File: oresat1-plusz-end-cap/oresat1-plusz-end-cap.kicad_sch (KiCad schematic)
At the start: 44 parts, among them J1 M55-7011242R, J2 U.FL-R-SMA, U1 RM3100, U2 RM3100

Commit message: routine push
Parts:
- added R16, R17, R18, R19: 121, oresat-passives:0603-C-NOSILK, symbol oresat-passives:R-US

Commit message: routine push
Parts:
- R17, R18: now not fitted
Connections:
- net +3.3v: now also R18.1, R19.1; no longer U1.28 (MISO/SA1)
- net GND: now also R16.2, R17.2; no longer U1.3 (SSN/SA0)
- net at R18.2: now also R16.1, U1.28 (MISO/SA1)
- net at R17.1: now also R19.2, U1.3 (SSN/SA0)
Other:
- moved on the sheet: R16, R19

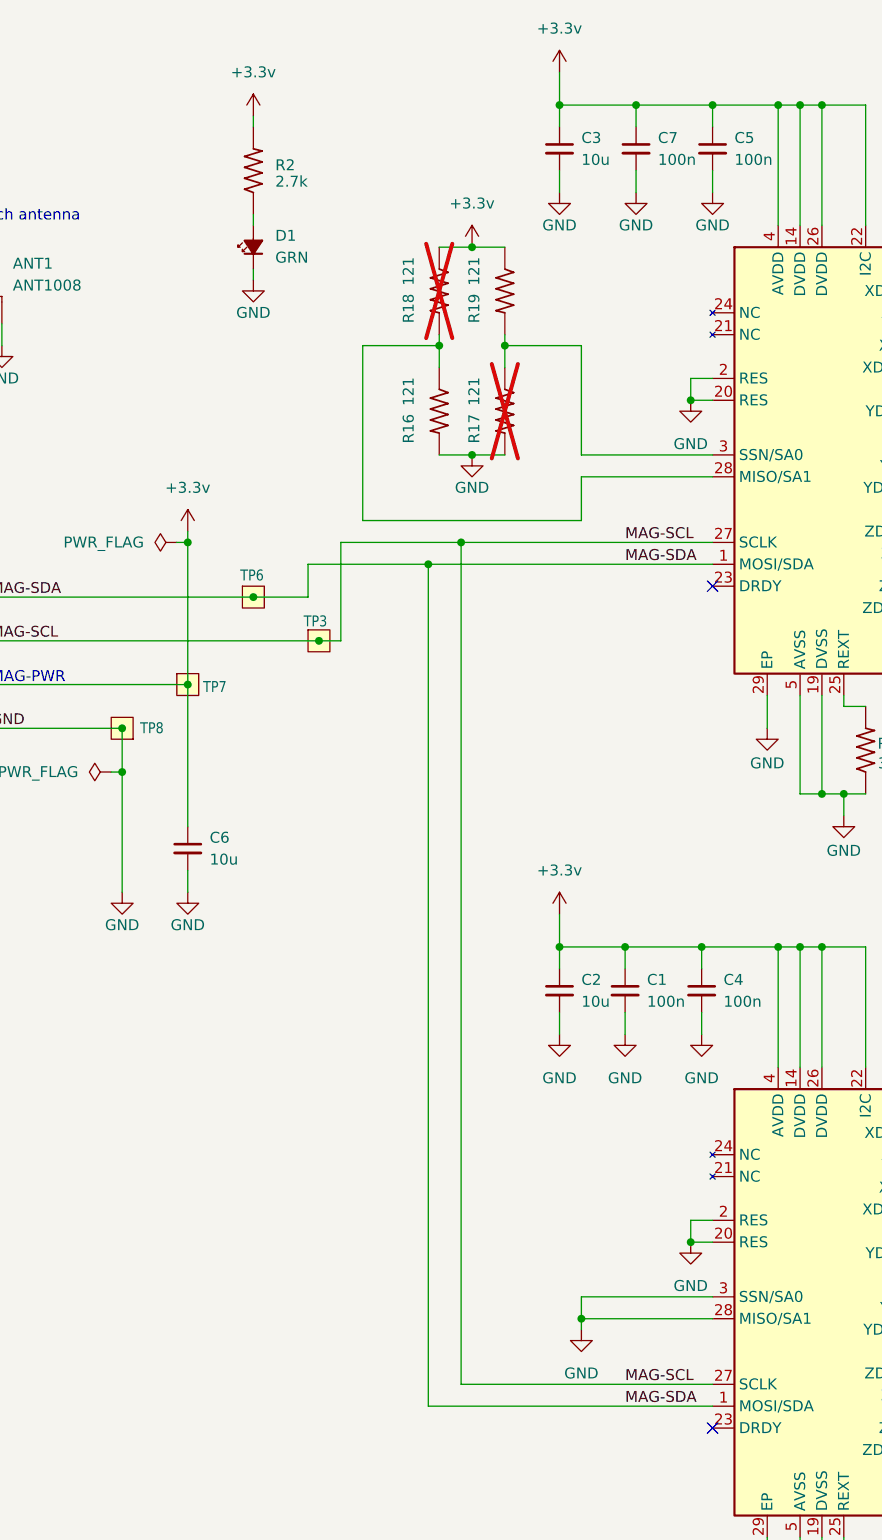
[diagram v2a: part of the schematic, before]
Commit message: Added releases, cleaned up PNI inductors, fixed ERCs and DRCs.
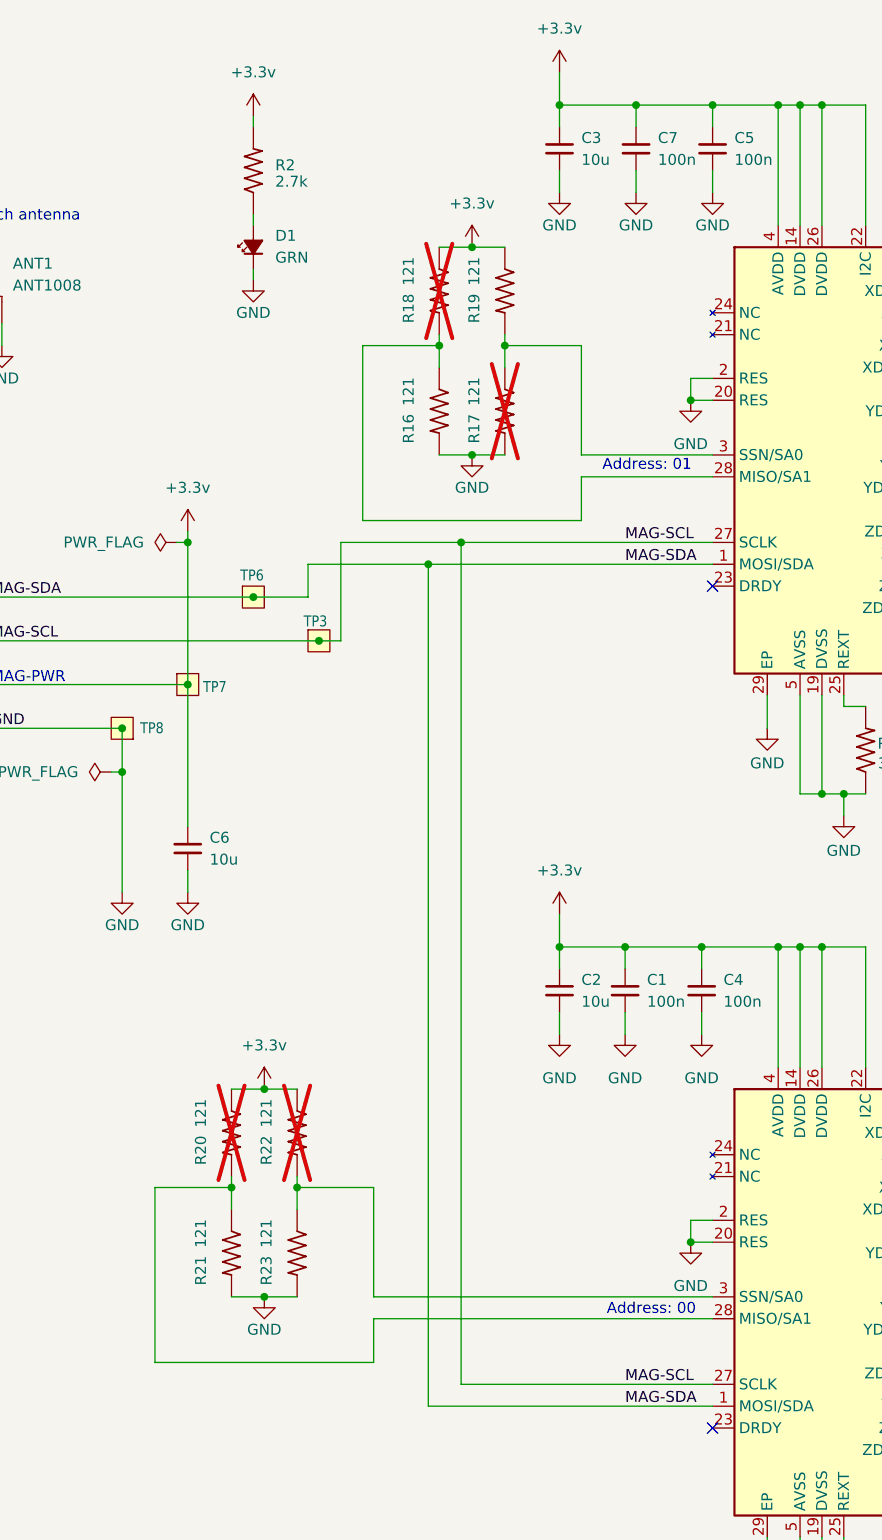
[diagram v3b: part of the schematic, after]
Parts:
- added R20, R21, R22, R23: 121, oresat-passives:0603-C-NOSILK, symbol oresat-passives:R-US
- ANT1: DIS (none) -> N/A; DST N/A -> (none)
- J2: DIS (none) -> DigiKey; DST DigiKey -> (none)
- L3, L4, L5, L7, L8, L9, U1, U2: DIS PNI -> N/A; DST N/A -> (none)
- R1, R10, R11, R12, R13, R14, R15, R16, R17, R18, R19, R2, R3, R4, R5, R6, R7, R8, R9: DST DigiKey -> (none)
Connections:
- net +3.3v: now also R20.1, R22.1
- net GND: now also R21.2, R23.2; no longer U2.28 (MISO/SA1), U2.3 (SSN/SA0)
- new net: R20.2, R21.1, U2.28 (MISO/SA1)
- new net: R22.2, R23.1, U2.3 (SSN/SA0)

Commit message: Updated paste for PNI sensors, better layout, polishing.
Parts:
- U1, U2: footprint oresat-misc:RM3100-MagI2C -> oresat-ics:U-PNI-RM3100-IC
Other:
- note added: "0805"
- note added: "3.3V and I2C signals are provide by the Mag card via the SPARE lines on the backplane: MAG-SDA = SPARE1 + SPARE2 MAG-SCL = SPARE3 + SPARE4 MAG-PWR = SPARE5 + SPARE6. These lines are delivered via the 12 pin connector on the +Z end card"
- note added: "All resistors 0603 1% and AEQ unless otherwise noted. All capacitors 0603 10% X5R Wv >= 25V and AEQ or better unless otherwise noted."
- note added: "DRVP/DRVN TRACES SHOULD BE EXACT EQUAL LENGTH PER SENSOR COUPLE (Why? this isn't in the datasheets?)"
- note added: "Z axis of RM3100 is "down" (the coils are set for North/East/Down) so for the +Z end cap, the Z sensor on the bottom of the board is actually pointed in the right direction!"
- note removed: "3.3V and I2C signals are provide by the Mag card via the SPARE lines on the backplane: MAG-SDA = SPARE1 + SPARE2 MAG-SCL = SPARE3 + SPARE4 MAG-PWR = SPARE5 + SPARE6. These lines are delivered via the 12 pin connector on the -Z end card"
- note removed: "All resistors 0603 1% unless otherwise noted. All capacitors 0603 x5R 16V or better unless otherwise noted."
- moved on the sheet: ANT1, C6, D1, J1, J2, R2, TP3, TP6, TP7, TP8

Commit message: Fixed documentation on mag address
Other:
- note added: "Address bits: 00"
- note added: "Address bits: 01"
- note added: "Address: 0x20"
- note added: "Address: 0x21"
- note removed: "Address: 00"
- note removed: "Address: 01"
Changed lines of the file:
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@@
 		)
 	)
-	(text "Address: 00"
-		(exclude_from_sim no)
-		(at 239.268 188.214 0)
+	(text "Address bits: 00"
+		(exclude_from_sim no)
+		(at 236.474 188.214 0)
 		(effects
 			(font
@@
 		)
 	)
-	(text "Address: 01"
+	(text "Address: 0x21"
 		(exclude_from_sim no)
 		(at 288.798 64.77 0)
@@
 		)
 	)
-	(text "Address: 00"
+	(text "Address: 0x20"
 		(exclude_from_sim no)
 		(at 290.322 158.496 0)
@@
 		)
 	)
-	(text "Address: 01"
-		(exclude_from_sim no)
-		(at 238.76 90.17 0)
-		(effects
-			(font
+	(text "Address bits: 01"
+		(exclude_from_sim no)
+		(at 237.236 90.424 0)
+		(effects
+			(font

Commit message: Spelling mistakes and better I2C documentation
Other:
- note added: "I2C Address: 0x20"
- note added: "I2C Address: 0x21"
- note removed: "Address: 0x20"
- note removed: "Address: 0x21"
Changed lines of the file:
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@@
 		)
 	)
-	(text "Address: 0x21"
+	(text "I2C Address: 0x21"
 		(exclude_from_sim no)
 		(at 288.798 64.77 0)
@@
 		)
 	)
-	(text "Address: 0x20"
+	(text "I2C Address: 0x20"
 		(exclude_from_sim no)
 		(at 290.322 158.496 0)
